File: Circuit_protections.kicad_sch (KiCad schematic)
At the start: 19 parts

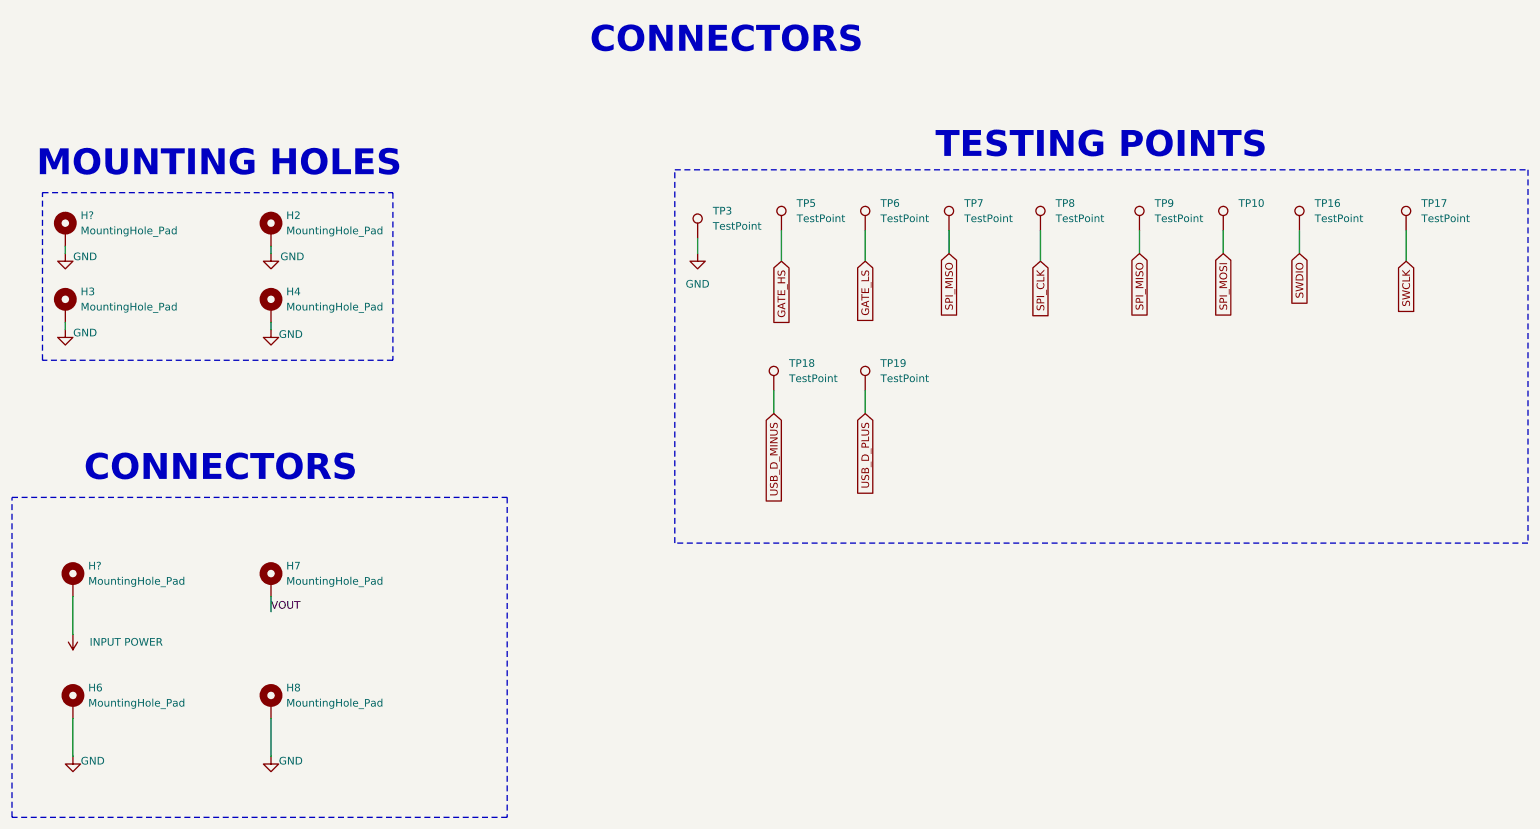
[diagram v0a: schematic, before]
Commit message: over-voltage protection added
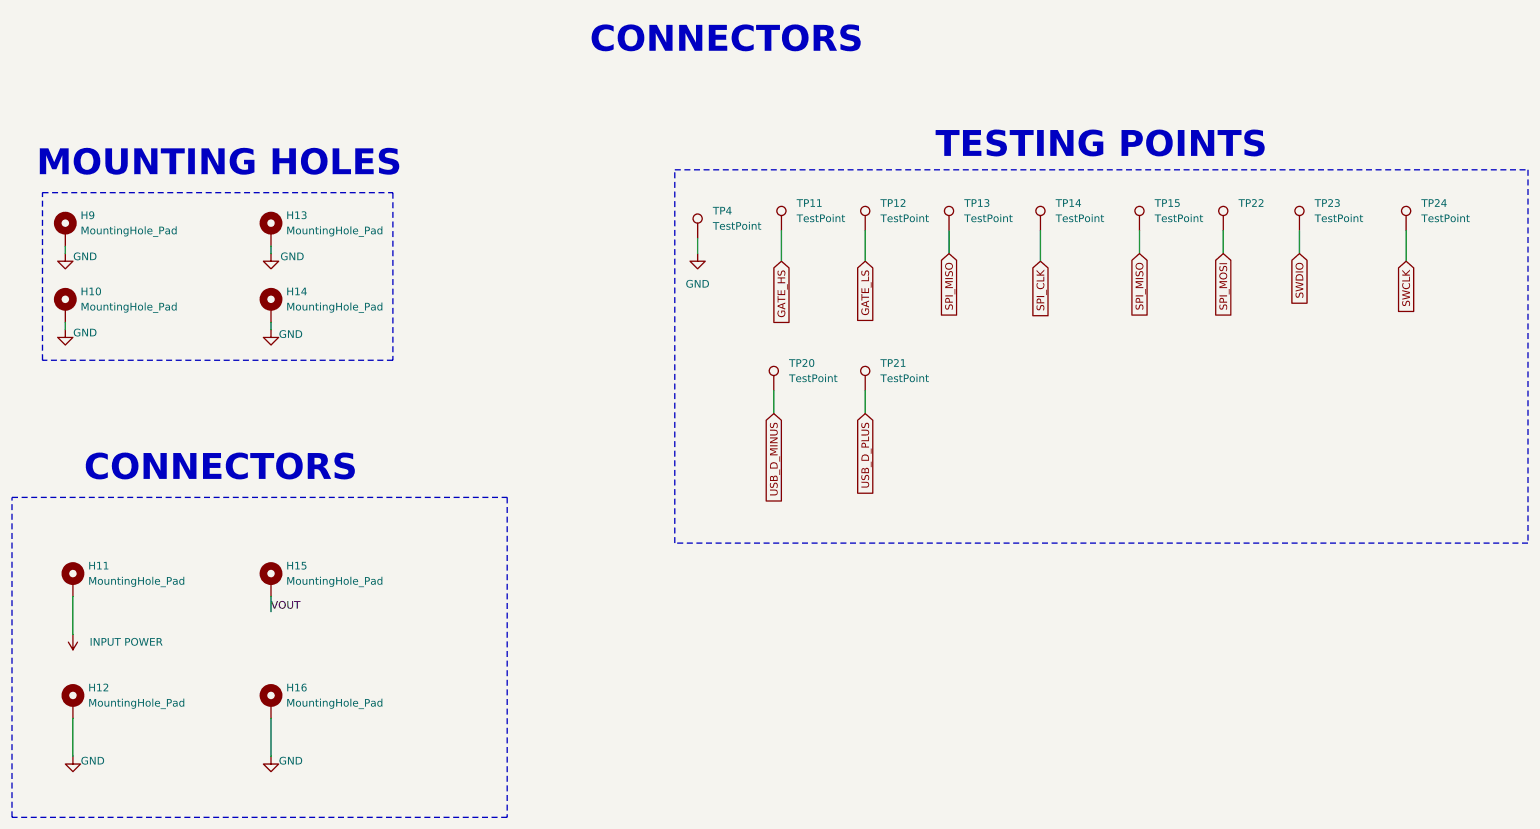
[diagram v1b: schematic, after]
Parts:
- gave numbers to parts that had none: 2
- renumbered H3 to H10, H6 to H12, H2 to H13, H4 to H14, H7 to H15, H8 to H16, TP5 to TP11, TP6 to TP12, TP7 to TP13, TP8 to TP14, TP9 to TP15, TP18 to TP20, TP19 to TP21, TP10 to TP22, TP16 to TP23, TP17 to TP24, TP3 to TP4

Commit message: Placement finished routing started
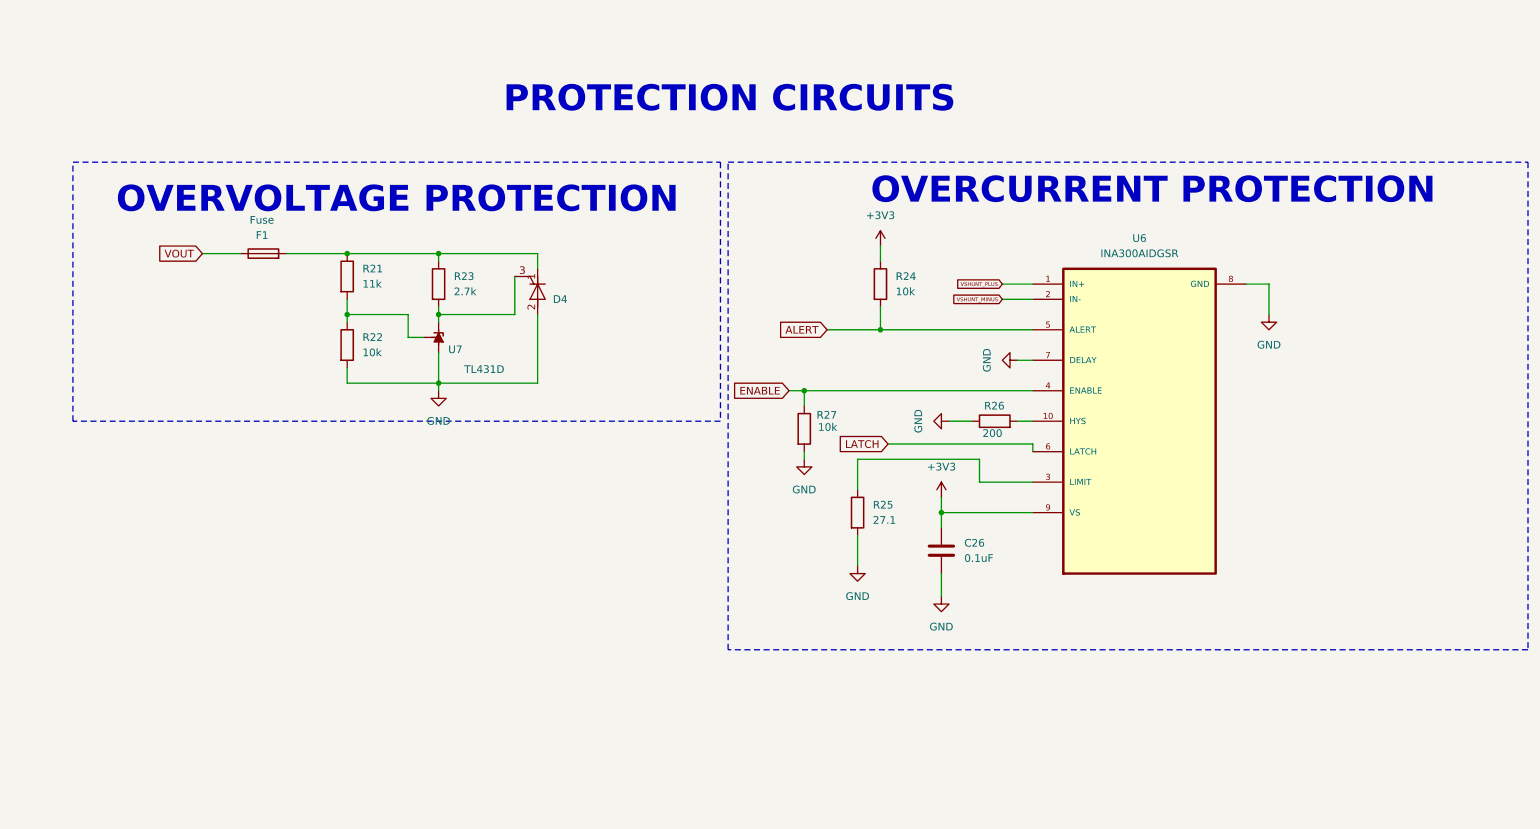
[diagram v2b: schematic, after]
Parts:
- removed H10, H13, H14, H9: MountingHole_Pad, MountingHole:MountingHole_3.2mm_M3_Pad, symbol Mechanical:MountingHole_Pad
- removed H11, H12, H15, H16: MountingHole_Pad, MountingHole:MountingHole_6.4mm_M6_ISO14580_Pad, symbol Mechanical:MountingHole_Pad
- removed TP11, TP12, TP13, TP14, TP15, TP22, TP4: TestPoint, TestPoint:TestPoint_Loop_D2.50mm_Drill1.0mm, symbol Connector:TestPoint
- removed TP20, TP21, TP23, TP24: TestPoint, TestPoint:TestPoint_Loop_D2.54mm_Drill1.5mm_Beaded, symbol Connector:TestPoint
- added C26: 0.1uF, Capacitor_SMD:C_0603_1608Metric_Pad1.08x0.95mm_HandSolder, symbol Device:C
- added D4: Q_SCR_KAG, Library:NYC222_THYRISTOR_FOOTPRINT, symbol Device:Q_SCR_KAG
- added F1: Fuse, Resistor_SMD:R_0603_1608Metric_Pad0.98x0.95mm_HandSolder, symbol Device:Fuse
- added R21: 11k, Resistor_SMD:R_0603_1608Metric_Pad0.98x0.95mm_HandSolder, symbol Device:R
- added R22: 10k, Resistor_SMD:R_0603_1608Metric_Pad0.98x0.95mm_HandSolder, symbol Device:R
- added R23: 2.7k, Resistor_SMD:R_0603_1608Metric_Pad0.98x0.95mm_HandSolder, symbol Device:R
- added R24, R27: 10k, Resistor_SMD:R_0402_1005Metric_Pad0.72x0.64mm_HandSolder, symbol Device:R
- added R25: 27.1, Resistor_SMD:R_0603_1608Metric_Pad0.98x0.95mm_HandSolder, symbol Device:R
- added R26: 200, Resistor_SMD:R_0402_1005Metric_Pad0.72x0.64mm_HandSolder, symbol Device:R
- added U6: INA300AIDGSR, Library:SOP50P490X110-10N-INA300, symbol INA300AIDGSR:INA300AIDGSR
- added U7: TL431D, Library:LM431, symbol Reference_Voltage:TL431D
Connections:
- net GND: now also C26.2, D4.2 (A), R22.2, R25.2, R26.1, R27.2, U6.7 (DELAY), U6.8 (GND), U7.2 (A), U7.3 (A), U7.6 (A), U7.7 (A)
- net VOUT: now also F1.1
- new net: R26.2, U6.10 (HYS)
- new net: R21.2, R22.1, U7.8 (REF)
- new net: D4.1 (K), F1.2, R21.1, R23.1
- new net: D4.3 (G), R23.2, U7.1 (K)
- new net: R25.1, U6.3 (LIMIT)
- new net +3V3: C26.1, R24.1, U6.9 (VS)
- new net ALERT: R24.2, U6.5 (ALERT)
- new net ENABLE: R27.1, U6.4 (ENABLE)
- new net LATCH: U6.6 (LATCH)
- new net VSHUNT_MINUS: U6.2 (IN-)
- new net VSHUNT_PLUS: U6.1 (IN+)
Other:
- note added: "OVERCURRENT PROTECTION"
- note added: "OVERVOLTAGE PROTECTION"
- note added: "PROTECTION CIRCUITS"
- note removed: "CONNECTORS"
- note removed: "MOUNTING HOLES"
- note removed: "TESTING POINTS"
